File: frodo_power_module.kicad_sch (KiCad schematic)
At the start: 78 parts, among them J1 Keystone 1098, J10 SWD Header, J2 Molex MicroFit 2x2, J3 Molex MicroFit 2x2, J4 Molex MicroFit 2x2, J5 Molex MicroFit 2x2, J6 Molex MicroFit 2x2, J7 JST-GH, J8 JST-GH, U1 STM32F042F6Px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

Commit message: modified schematic
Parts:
- removed JP1: SolderJumper_2_Open, Jumper:SolderJumper-2_P1.3mm_Open_RoundedPad1.0x1.5mm, symbol Jumper:SolderJumper_2_Open
- added J11: Conn_01x04, symbol Connector_Generic:Conn_01x04
- added J13, J9: Conn_01x06, symbol Connector_Generic:Conn_01x06
- J1: value Keystone 1098 -> Keystone 1048; footprint frodo_power_module:keystone_1098 -> frodo_power_module:keystone_1048; Part# 1098 -> 1048
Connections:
- net CAN- is gone; now on net CAN+: J7.3 (Pin_3), J8.3 (Pin_3), R1.2, U6.6 (CANL)
- net +3V3: no longer R25.1, R26.1
- net +VSW: now also J11.1 (Pin_1), J11.2 (Pin_2), J13.3 (Pin_3), J9.3 (Pin_3)
- net CAN+: now also J13.5 (Pin_5), J13.6 (Pin_6), J9.5 (Pin_5), J9.6 (Pin_6)
- net GND: now also J11.3 (Pin_3), J11.4 (Pin_4), J13.2 (Pin_2), J13.4 (Pin_4), J9.2 (Pin_2), J9.4 (Pin_4)
- net VDC: now also J13.1 (Pin_1), J9.1 (Pin_1)
- net at C12.1, D1.1 (K), U4.1 (IN): now also R25.1, R26.1
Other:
- note added: "Back Side Connectors"
- note added: "Diode resistor: (12V-3V)/10mA = 900 Ohm"
- note added: "Top Side Connectors"
- note added: "Was ist aber hier der Main Bus Connector und was sind die Konnektoren zum Flight Computer weil nach Valispace sindd die 2x2 Konnektoren aber ohne CAN+ und CAN-"
- note removed: "Allows bypassing (unpopulated) charger completely to directly apply charging voltage to battery, for example when used in other rockets (AESIR)."
- moved on the sheet: C13, C18, C19, D2, D3, F2, F3, H1, H2, H3, H4, J2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

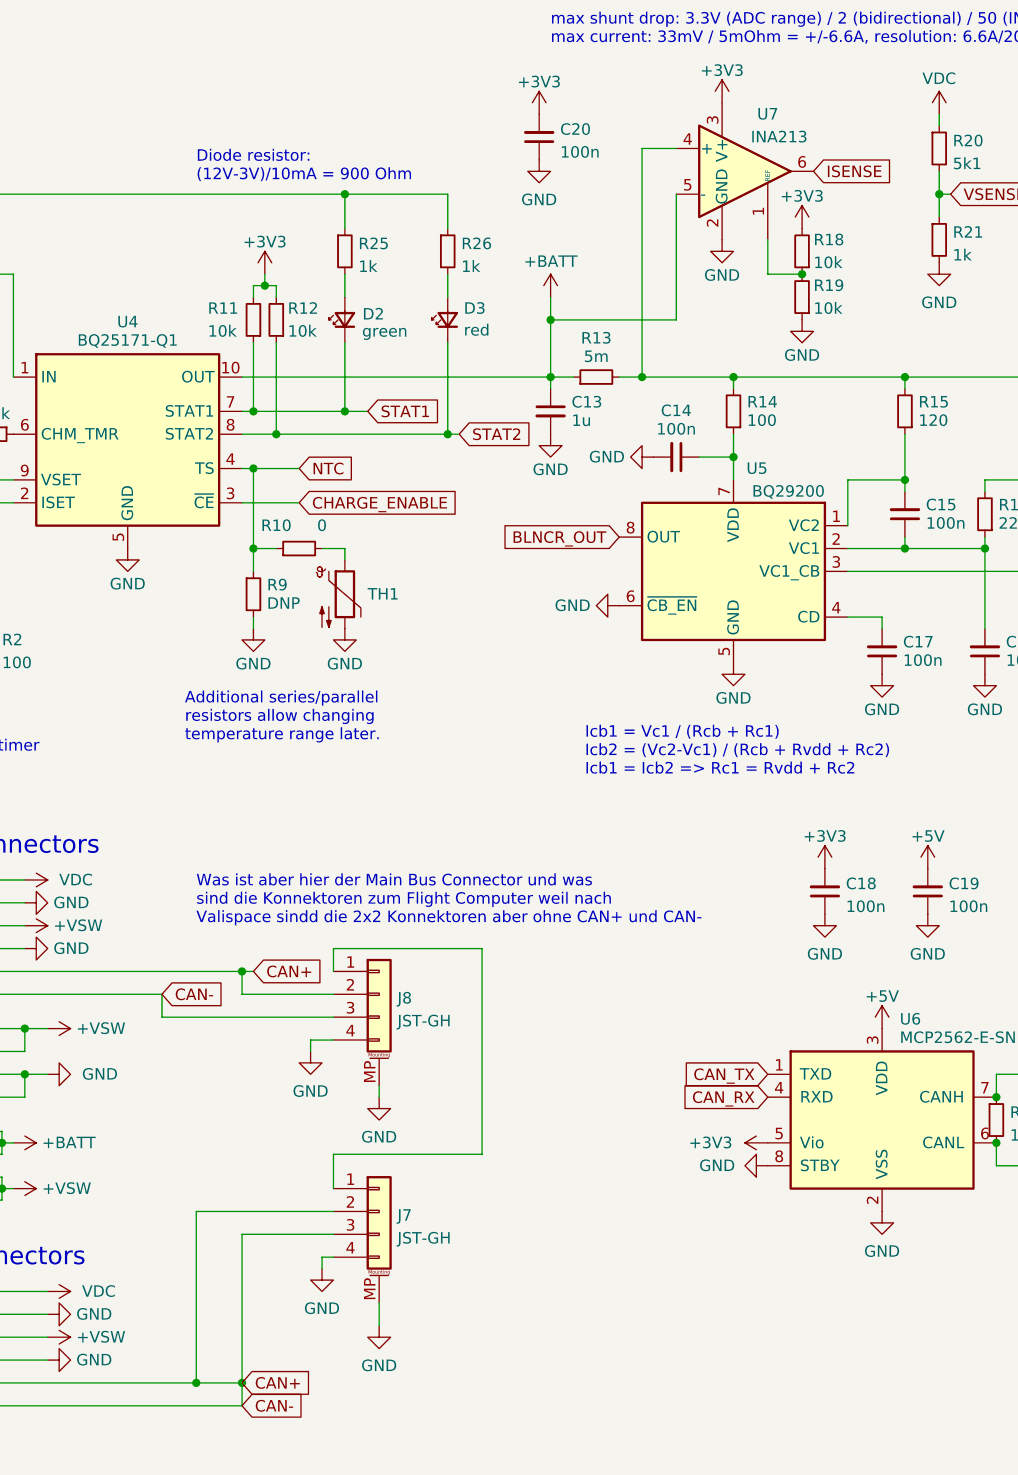
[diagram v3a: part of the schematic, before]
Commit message: changed battery connector type, removed breakwrie, Iset resisrtor config and placed LEDS on main power supply
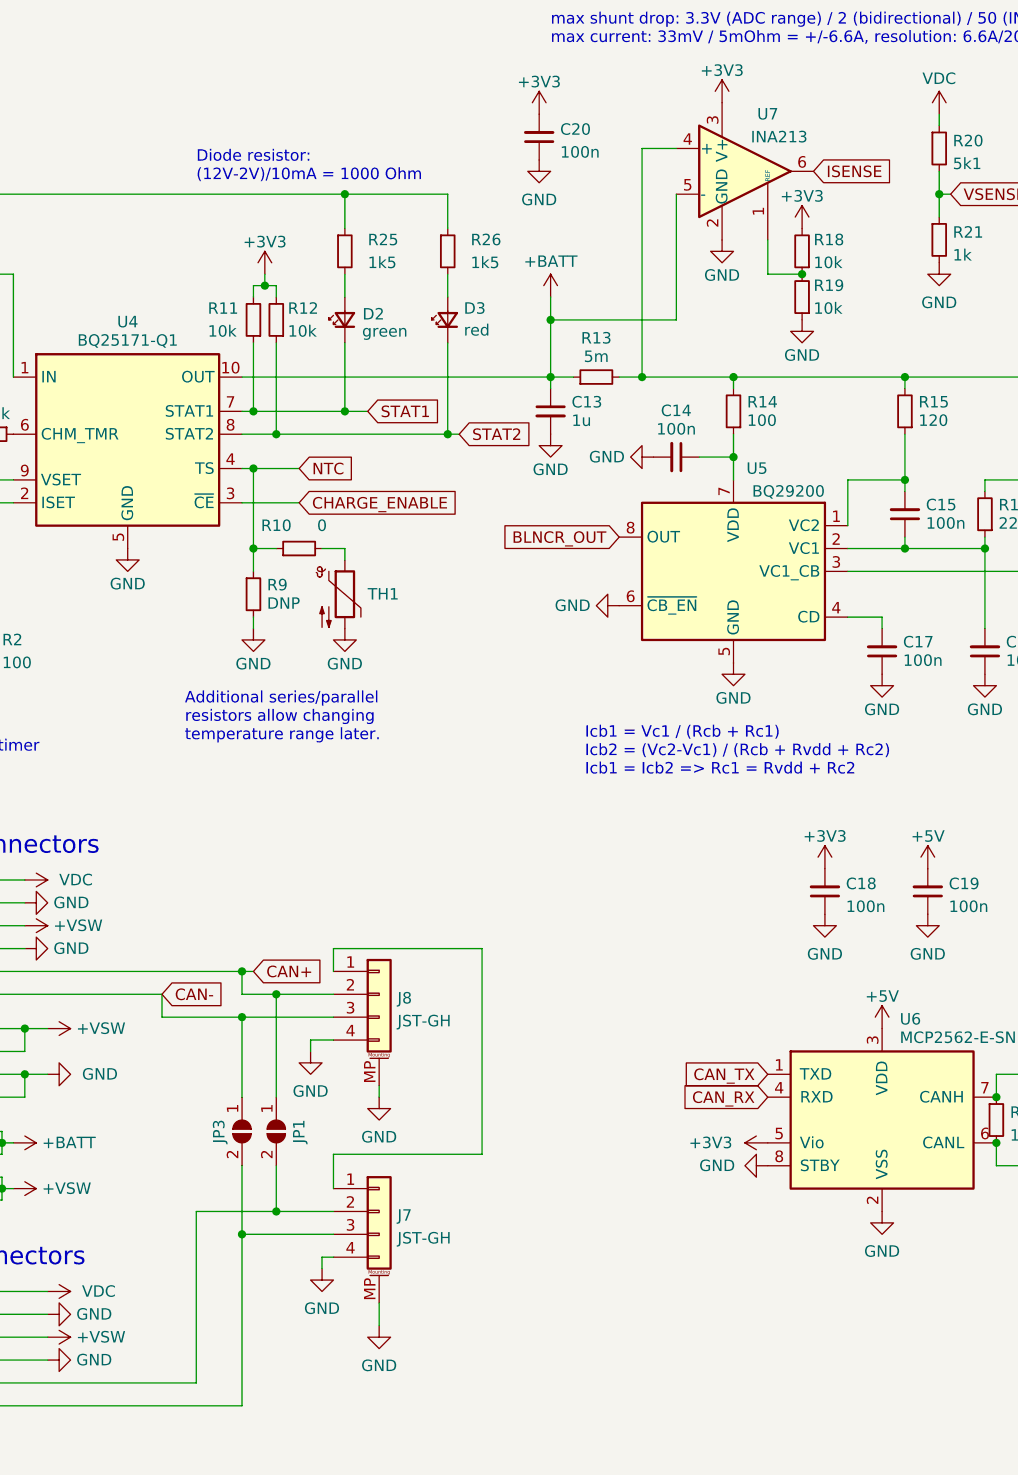
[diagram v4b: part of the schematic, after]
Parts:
- added JP1, JP3: SolderJumper_2_Open, Jumper:SolderJumper-2_P1.3mm_Open_RoundedPad1.0x1.5mm, symbol Jumper:SolderJumper_2_Open
- R25, R26: value 1k -> 1k5
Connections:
- net CAN+: now also JP1.1 (A); no longer J13.5 (Pin_5), J13.6 (Pin_6), J7.2 (Pin_2), J7.3 (Pin_3), J8.3 (Pin_3), J9.6 (Pin_6), R1.2, U6.6 (CANL)
- new net: J13.6 (Pin_6), J7.3 (Pin_3), JP3.2 (B)
- new net: J13.5 (Pin_5), J7.2 (Pin_2), JP1.2 (B)
- new net CAN-: J8.3 (Pin_3), J9.6 (Pin_6), JP3.1 (A), R1.2, U6.6 (CANL)
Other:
- note added: "Diode resistor: (12V-2V)/10mA = 1000 Ohm"
- note removed: "Diode resistor: (12V-3V)/10mA = 900 Ohm"
- note removed: "Was ist aber hier der Main Bus Connector und was sind die Konnektoren zum Flight Computer weil nach Valispace sindd die 2x2 Konnektoren aber ohne CAN+ und CAN-"
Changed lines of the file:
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@@
   (junction (at 34.29 35.56) (diameter 0) (color 0 0 0 0)
   )
+  (junction (at 71.12 124.46) (diameter 0) (color 0 0 0 0)
+  )
   (junction (at -15.24 153.67) (diameter 0) (color 0 0 0 0)
   )
@@
   (junction (at 34.29 44.45) (diameter 0) (color 0 0 0 0)
   )
+  (junction (at 71.12 148.59) (diameter 0) (color 0 0 0 0)
+  )
   (junction (at 144.78 35.56) (diameter 0) (color 0 0 0 0)
   )
@@
   (junction (at 255.27 36.83) (diameter 0) (color 0 0 0 0)
   )
-  (junction (at 62.23 167.64) (diameter 0) (color 0 0 0 0)
-  )
   (junction (at 181.61 115.57) (diameter 0) (color 0 0 0 0)
   )
@@
   (junction (at 223.52 31.75) (diameter 0) (color 0 0 0 0)
   )
+  (junction (at 67.31 151.13) (diameter 0) (color 0 0 0 0)
+  )
   (junction (at 34.29 83.82) (diameter 0) (color 0 0 0 0)
   )
@@
   (junction (at 71.12 62.23) (diameter 0) (color 0 0 0 0)
   )
+  (junction (at 67.31 127) (diameter 0) (color 0 0 0 0)
+  )
   (junction (at 149.86 74.93) (diameter 0) (color 0 0 0 0)
   )
@@
   (junction (at 121.92 64.77) (diameter 0) (color 0 0 0 0)
   )
-  (junction (at 67.31 167.64) (diameter 0) (color 0 0 0 0)
-  )
   (junction (at 245.11 66.04) (diameter 0) (color 0 0 0 0)
   )
@@
     (stroke (width 0) (type default))
   )
-  (wire (pts (xy 62.23 167.64) (xy 67.31 167.64))
-    (stroke (width 0) (type default))
-  )
   (wire (pts (xy 121.92 62.23) (xy 121.92 64.77))
     (stroke (width 0) (type default))
@@
     (stroke (width 0) (type default))
   )
-  (wire (pts (xy 67.31 167.64) (xy 67.31 170.18))
+  (wire (pts (xy 67.31 151.13) (xy 67.31 170.18))
     (stroke (width 0) (type default))
   )
@@
     (stroke (width 0) (type default))
   )
-  (wire (pts (xy 67.31 124.46) (xy 77.47 124.46))
+  (wire (pts (xy 67.31 124.46) (xy 71.12 124.46))
     (stroke (width 0) (type default))
   )
@@
     (stroke (width 0) (type default))
   )
-  (wire (pts (xy 67.31 151.13) (xy 67.31 167.64))
-    (stroke (width 0) (type default))
-  )
   (wire (pts (xy 111.76 55.88) (xy 121.92 55.88))
     (stroke (width 0) (type default))
@@
     (stroke (width 0) (type default))
   )
+  (wire (pts (xy 71.12 124.46) (xy 77.47 124.46))
+    (stroke (width 0) (type default))
+  )
   (wire (pts (xy 134.62 67.31) (xy 134.62 72.39))
     (stroke (width 0) (type default))
@@
     (stroke (width 0) (type default))
   )
+  (wire (pts (xy 67.31 127) (xy 77.47 127))
+    (stroke (width 0) (type default))
+  )
   (wire (pts (xy -13.97 142.24) (xy -15.24 142.24))
     (stroke (width 0) (type default))
@@
     (stroke (width 0) (type default))
   )
+  (wire (pts (xy 71.12 148.59) (xy 77.47 148.59))
+    (stroke (width 0) (type default))
+  )
   (wire (pts (xy 67.31 121.92) (xy 67.31 124.46))
     (stroke (width 0) (type default))
@@
     (stroke (width 0) (type default))
   )
+  (wire (pts (xy 67.31 143.51) (xy 67.31 151.13))
+    (stroke (width 0) (type default))
+  )
   (wire (pts (xy 157.48 68.58) (xy 157.48 67.31))
     (stroke (width 0) (type default))
@@
     (stroke (width 0) (type default))
   )
+  (wire (pts (xy 71.12 143.51) (xy 71.12 148.59))
+    (stroke (width 0) (type default))
+  )
   (wire (pts (xy 140.97 55.88) (xy 165.1 55.88))
     (stroke (width 0) (type default))
@@
     (stroke (width 0) (type default))
   )
+  (wire (pts (xy 71.12 124.46) (xy 71.12 135.89))
+    (stroke (width 0) (type default))
+  )
   (wire (pts (xy -15.24 163.83) (xy -16.51 163.83))
     (stroke (width 0) (type default))
@@
     (stroke (width 0) (type default))
   )
+  (wire (pts (xy 67.31 127) (xy 67.31 135.89))
+    (stroke (width 0) (type default))
+  )
   (wire (pts (xy -16.51 129.54) (xy -15.24 129.54))
     (stroke (width 0) (type default))
@@
     (stroke (width 0) (type default))
   )
-  (wire (pts (xy 62.23 148.59) (xy 77.47 148.59))
+  (wire (pts (xy 62.23 148.59) (xy 71.12 148.59))
     (stroke (width 0) (type default))
   )
@@
     (stroke (width 0) (type default))
   )
-  (wire (pts (xy 58.42 127) (xy 77.47 127))
+  (wire (pts (xy 58.42 127) (xy 67.31 127))
     (stroke (width 0) (type default))
   )
@@
     (effects (font (size 1.27 1.27)) (justify left bottom))
   )
-  (text "Diode resistor:\n(12V-3V)/10mA = 900 Ohm" (at 62.23 34.29 0)
-    (effects (font (size 1.27 1.27)) (justify left bottom))
-  )
-  (text "Was ist aber hier der Main Bus Connector und was \nsind die Konnektoren zum Flight Computer weil nach\nValispace sindd die 2x2 Konnektoren aber ohne CAN+ und CAN-"
-    (at 62.23 116.84 0)
+  (text "Diode resistor:\n(12V-2V)/10mA = 1000 Ohm" (at 62.23 34.29 0)
     (effects (font (size 1.27 1.27)) (justify left bottom))
   )
@@
     )
   )
-  (global_label "CAN-" (shape input) (at 67.31 170.18 0) (fields_autoplaced)
-    (effects (font (size 1.27 1.27)) (justify left))
-    (property "Intersheetrefs" "${INTERSHEET_REFS}" (at 74.9845 170.1006 0)
-      (effects (font (size 1.27 1.27)) (justify left) hide)
-    )
-  )
   (global_label "STAT2" (shape input) (at 91.44 62.23 0) (fields_autoplaced)
     (effects (font (size 1.27 1.27)) (justify left))
@@
     )
   )
-  (global_label "CAN+" (shape input) (at 67.31 167.64 0) (fields_autoplaced)
-    (effects (font (size 1.27 1.27)) (justify left))
-    (property "Intersheetrefs" "${INTERSHEET_REFS}" (at 74.9845 167.5606 0)
-      (effects (font (size 1.27 1.27)) (justify left) hide)
-    )
-  )
   (global_label "OSC_OUT" (shape input) (at 219.71 102.87 180) (fields_autoplaced)
     (effects (font (size 1.27 1.27)) (justify right))
@@
   (symbol (lib_id "Device:R_Small") (at 90.17 41.91 0) (unit 1)
     (in_bom yes) (on_board yes) (dnp no) (fields_autoplaced)
-    (property "Reference" "R26" (at 91.6686 41.0753 0)
+    (property "Reference" "R26" (at 92.71 40.64 0)
       (effects (font (size 1.27 1.27)) (justify left))
     )
-    (property "Value" "1k" (at 91.6686 43.6122 0)
+    (property "Value" "1k5" (at 92.71 43.18 0)
       (effects (font (size 1.27 1.27)) (justify left))
     )
@@
     )
   )
+  (symbol (lib_id "Jumper:SolderJumper_2_Open") (at 67.31 139.7 90) (mirror x) (unit 1)
+    (in_bom yes) (on_board yes) (dnp no)
+    (property "Reference" "JP3" (at 64.77 139.7 0)
+      (effects (font (size 1.27 1.27)))
+    )
+    (property "Value" "SolderJumper_2_Open" (at 64.889 139.7 0)
+      (effects (font (size 1.27 1.27)) hide)
+    )
+    (property "Footprint" "Jumper:SolderJumper-2_P1.3mm_Open_RoundedPad1.0x1.5mm" (at 67.31 139.7 0)
+      (effects (font (size 1.27 1.27)) hide)
+    )
+    (property "Datasheet" "~" (at 67.31 139.7 0)
+      (effects (font (size 1.27 1.27)) hide)
+    )
+    (property "Manufacturer" "N/A" (at 67.31 139.7 0)
+      (effects (font (size 1.27 1.27)) hide)
+    )
+    (property "Part#" "N/A" (at 67.31 139.7 0)
+      (effects (font (size 1.27 1.27)) hide)
+    )
+    (property "DigiKey#" "N/A" (at 67.31 139.7 0)
+      (effects (font (size 1.27 1.27)) hide)
+    )
+    (property "LCSC#" "N/A" (at 67.31 139.7 0)
+      (effects (font (size 1.27 1.27)) hide)
+    )
+    (pin "1")
+    (pin "2")
+    (instances
+      (project "frodo_power_module"
+        (path "/afc8cbd3-9ea8-40a2-afae-ed6bd0fe7e6e"
+          (reference "JP3") (unit 1)
+        )
+      )
+    )
+  )
   (symbol (lib_id "Device:Polyfuse_Small") (at -3.175 161.29 90) (unit 1)
     (in_bom yes) (on_board yes) (dnp no) (fields_autoplaced)
@@
     )
   )
+  (symbol (lib_id "Jumper:SolderJumper_2_Open") (at 71.12 139.7 270) (unit 1)
+    (in_bom yes) (on_board yes) (dnp no)
+    (property "Reference" "JP1" (at 73.66 139.7 0)
+      (effects (font (size 1.27 1.27)))
+    )
+    (property "Value" "SolderJumper_2_Open" (at 73.541 139.7 0)
+      (effects (font (size 1.27 1.27)) hide)
+    )
+    (property "Footprint" "Jumper:SolderJumper-2_P1.3mm_Open_RoundedPad1.0x1.5mm" (at 71.12 139.7 0)
+      (effects (font (size 1.27 1.27)) hide)
+    )
+    (property "Datasheet" "~" (at 71.12 139.7 0)
+      (effects (font (size 1.27 1.27)) hide)
+    )
+    (property "Manufacturer" "N/A" (at 71.12 139.7 0)
+      (effects (font (size 1.27 1.27)) hide)
+    )
+    (property "Part#" "N/A" (at 71.12 139.7 0)
+      (effects (font (size 1.27 1.27)) hide)
+    )
+    (property "DigiKey#" "N/A" (at 71.12 139.7 0)
+      (effects (font (size 1.27 1.27)) hide)
+    )
+    (property "LCSC#" "N/A" (at 71.12 139.7 0)
+      (effects (font (size 1.27 1.27)) hide)
+    )
+    (pin "1")
+    (pin "2")
+    (instances
+      (project "frodo_power_module"
+        (path "/afc8cbd3-9ea8-40a2-afae-ed6bd0fe7e6e"
+          (reference "JP1") (unit 1)
+        )
+      )
+    )
+  )
   (symbol (lib_id "power:+5V") (at 223.52 31.75 0) (unit 1)
     (in_bom yes) (on_board yes) (dnp no) (fields_autoplaced)
@@
   (symbol (lib_id "Device:R_Small") (at 78.74 41.91 0) (unit 1)
     (in_bom yes) (on_board yes) (dnp no) (fields_autoplaced)
-    (property "Reference" "R25" (at 80.2386 41.0753 0)
+    (property "Reference" "R25" (at 81.28 40.64 0)
       (effects (font (size 1.27 1.27)) (justify left))
     )
-    (property "Value" "1k" (at 80.2386 43.6122 0)
+    (property "Value" "1k5" (at 81.28 43.18 0)
       (effects (font (size 1.27 1.27)) (justify left))
     )

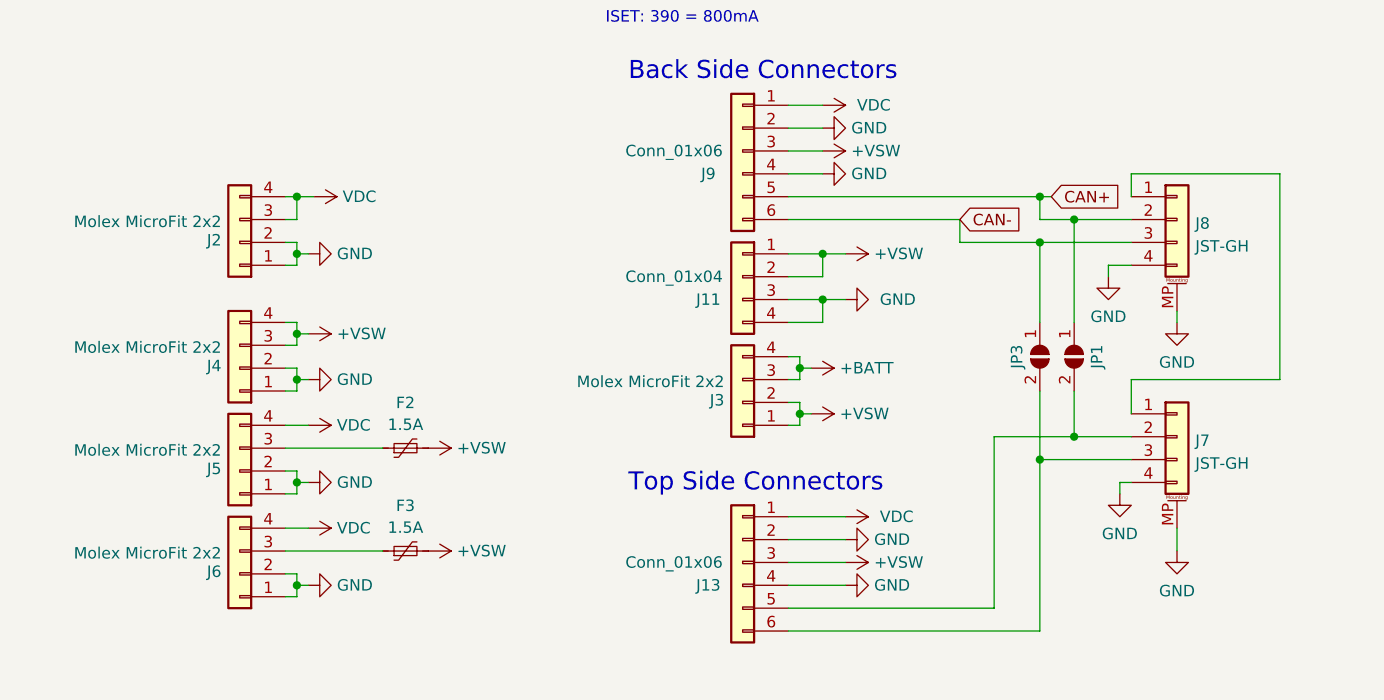
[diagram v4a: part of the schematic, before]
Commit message: removed other connectors
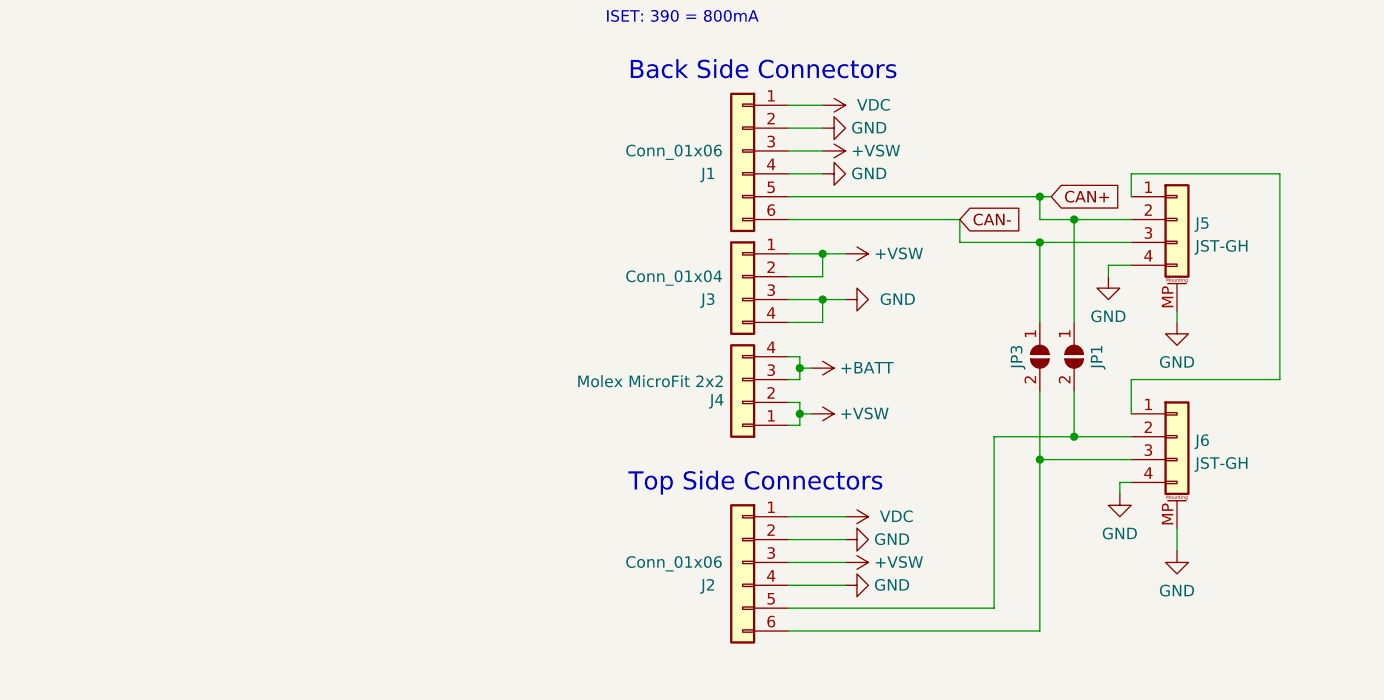
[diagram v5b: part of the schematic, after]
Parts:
- removed F2, F3: 1.5A, Fuse:Fuse_1206_3216Metric, symbol Device:Polyfuse_Small
- removed J2, J4, J5, J6: Molex MicroFit 2x2, Connector_Molex:Molex_Micro-Fit_3.0_43045-0400_2x02_P3.00mm_Horizontal, symbol Connector_Generic:Conn_01x04
- renumbered J9 to J1, J13 to J2, J11 to J3, J3 to J4, J8 to J5, J7 to J6

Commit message: updated
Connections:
- net +VSW: now also J1.5 (Pin_5), J2.5 (Pin_5); no longer J1.3 (Pin_3), J2.3 (Pin_3)
- net CAN+: now also J1.6 (Pin_6); no longer J1.5 (Pin_5)
- net CAN-: now also J1.3 (Pin_3); no longer J1.6 (Pin_6)
- net GND: now also J1.1 (Pin_1), J2.1 (Pin_1); no longer J1.4 (Pin_4), J2.4 (Pin_4)
- net VDC: now also J1.4 (Pin_4), J2.4 (Pin_4); no longer J1.1 (Pin_1), J2.1 (Pin_1)
- net at J6.3 (Pin_3), JP3.2 (B): now also J2.3 (Pin_3); no longer J2.6 (Pin_6)
- net at J6.2 (Pin_2), JP1.2 (B): now also J2.6 (Pin_6); no longer J2.5 (Pin_5)
